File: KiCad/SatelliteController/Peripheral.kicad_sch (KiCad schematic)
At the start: 7 parts, among them J11 RJ45, J15 CONN_AUDIO, J16 CONN_SPEAKER, U2 24LC256, U6 DFPlayer, U7 LTC485CN8#PBF

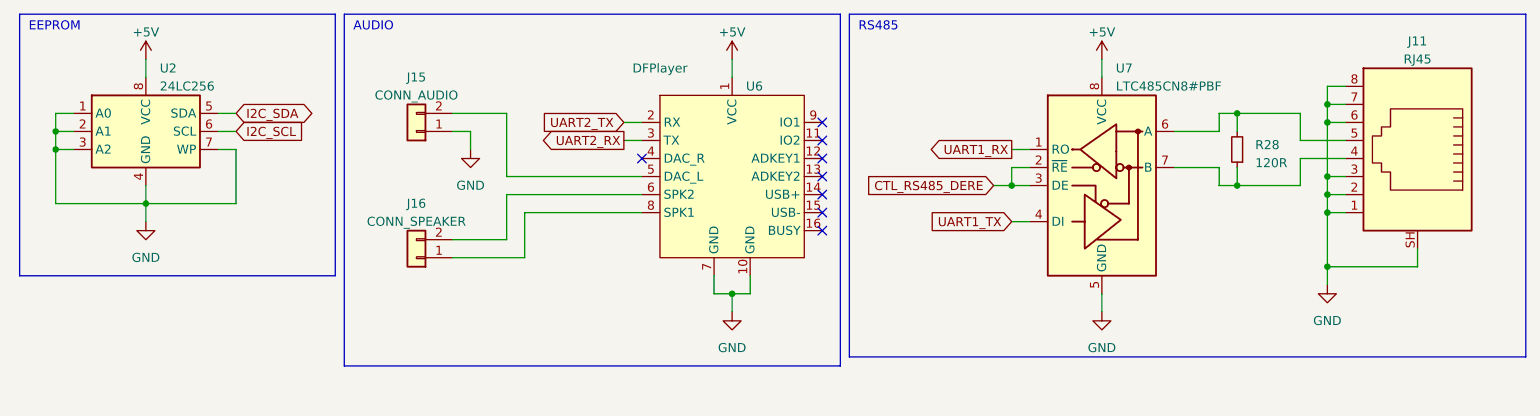
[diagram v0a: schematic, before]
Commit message: 圧力センサとの接続部を追加
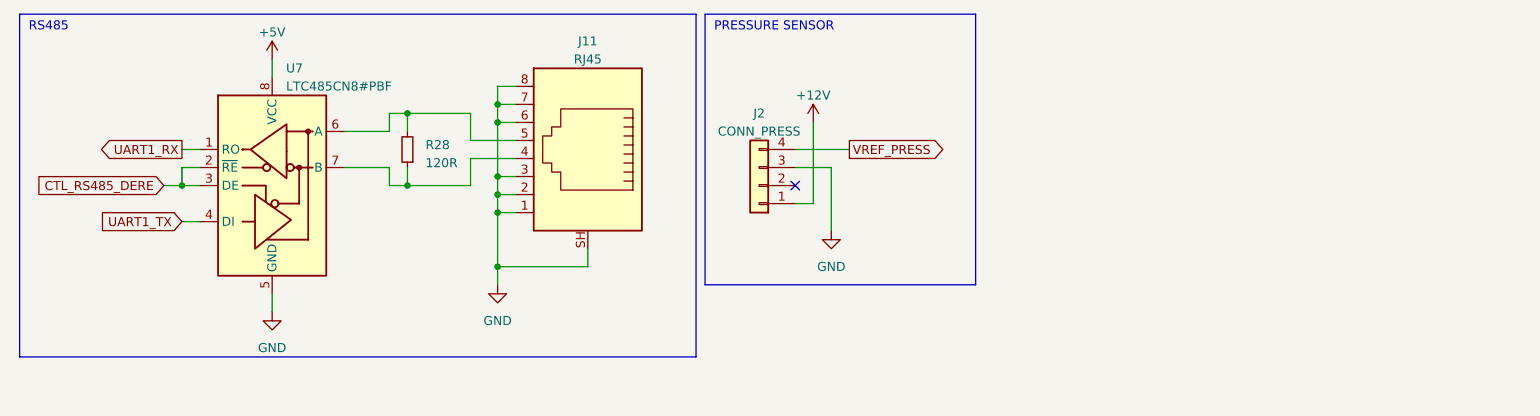
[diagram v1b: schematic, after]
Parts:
- removed J15: CONN_AUDIO, TSRP_TerminalBlock_Alphaplus:TB401-1-2-E, symbol Connector_Generic:Conn_01x02
- removed J16: CONN_SPEAKER, TSRP_TerminalBlock_Alphaplus:TB401-1-2-E, symbol Connector_Generic:Conn_01x02
- removed U2: 24LC256, Package_DIP:DIP-8_W7.62mm, symbol Memory_EEPROM:24LC256
- removed U6: DFPlayer, TSRP_Module:DFPlayer-mini, symbol TSRP_Module:DFPlayer-mini
- added J2: CONN_PRESS, TSRP_TerminalBlock_Alphaplus:TB401-1-4-E, symbol Connector_Generic:Conn_01x04
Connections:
- net GND: now also J2.3 (Pin_3)
- new net +12V: J2.1 (Pin_1)
- new net VREF_PRESS: J2.4 (Pin_4)
- no-connect marks 8 -> 1
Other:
- note added: "PRESSURE SENSOR"
- note removed: "AUDIO"
- note removed: "EEPROM"
- moved on the sheet: J11, R28, U7

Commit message: ランコンのKiCadプロジェクトをコピーしてサテコンを作成
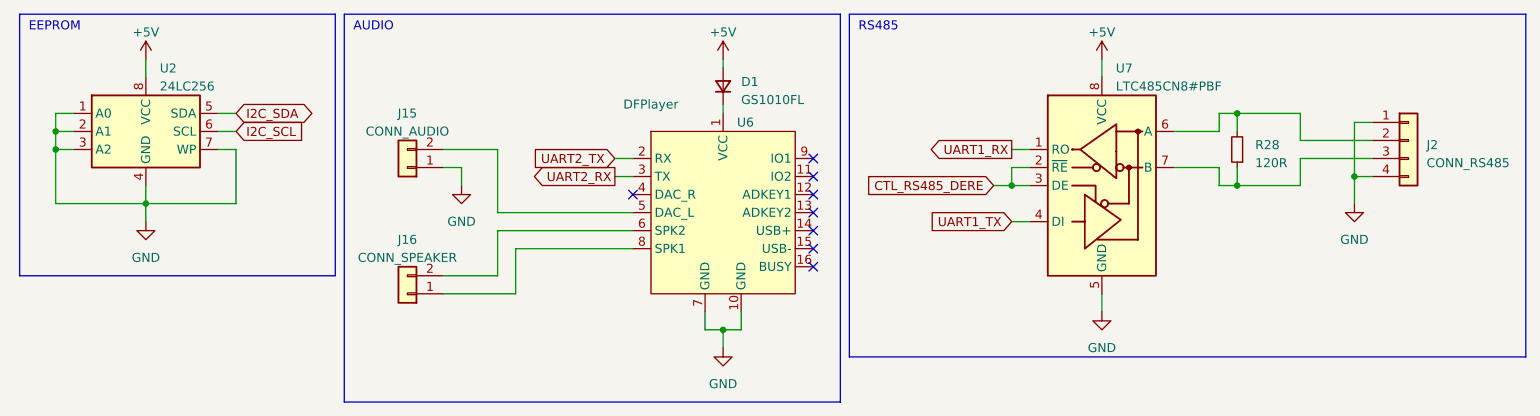
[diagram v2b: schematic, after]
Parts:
- removed J11: RJ45, Connector_RJ:RJ45_Wuerth_7499010001A_Horizontal, symbol Connector:RJ45_Shielded
- added D1: GS1010FL, Diode_SMD:D_SOD-123F, symbol Device:D_Small
- added J15: CONN_AUDIO, TSRP_TerminalBlock_Alphaplus:TB401-1-2-E, symbol Connector_Generic:Conn_01x02
- added J16: CONN_SPEAKER, TSRP_TerminalBlock_Alphaplus:TB401-1-2-E, symbol Connector_Generic:Conn_01x02
- added U2: 24LC256, Package_DIP:DIP-8_W7.62mm, symbol Memory_EEPROM:24LC256
- added U6: DFPlayer, TSRP_Module:DFPlayer-mini, symbol TSRP_Module:DFPlayer-mini
- J2: value CONN_PRESS -> CONN_RS485
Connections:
- net +12V is gone; now on net GND: J2.1 (Pin_1)
- net VREF_PRESS is gone; now on net GND: J2.4 (Pin_4)
- net +5V: now also D1.2 (A), U2.8 (VCC)
- net GND: now also J15.1 (Pin_1), U2.1 (A0), U2.2 (A1), U2.3 (A2), U2.4 (GND), U2.7 (WP), U6.10 (GND), U6.7 (GND); no longer J2.3 (Pin_3)
- net at R28.1, U7.7 (B): now also J2.3 (Pin_3)
- net at R28.2, U7.6 (A): now also J2.2 (Pin_2)
- new net: J16.1 (Pin_1), U6.8 (SPK1)
- new net: J16.2 (Pin_2), U6.6 (SPK2)
- new net: D1.1 (K), U6.1 (VCC)
- new net: J15.2 (Pin_2), U6.5 (DAC_L)
- new net I2C_SCL: U2.6 (SCL)
- new net I2C_SDA: U2.5 (SDA)
- new net UART2_RX: U6.3 (TX)
- new net UART2_TX: U6.2 (RX)
- no-connect marks 1 -> 8
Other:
- note added: "AUDIO"
- note added: "EEPROM"
- note removed: "PRESSURE SENSOR"
- moved on the sheet: R28, U7

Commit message: 音声完成を削除
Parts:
- removed D1: GS1010FL, Diode_SMD:D_SOD-123F, symbol Device:D_Small
- removed J15: CONN_AUDIO, TSRP_TerminalBlock_Alphaplus:TB401-1-2-E, symbol Connector_Generic:Conn_01x02
- removed J16: CONN_SPEAKER, TSRP_TerminalBlock_Alphaplus:TB401-1-2-E, symbol Connector_Generic:Conn_01x02
- removed U6: DFPlayer, TSRP_Module:DFPlayer-mini, symbol TSRP_Module:DFPlayer-mini
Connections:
- no-connect marks 8 -> 0
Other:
- note removed: "AUDIO"

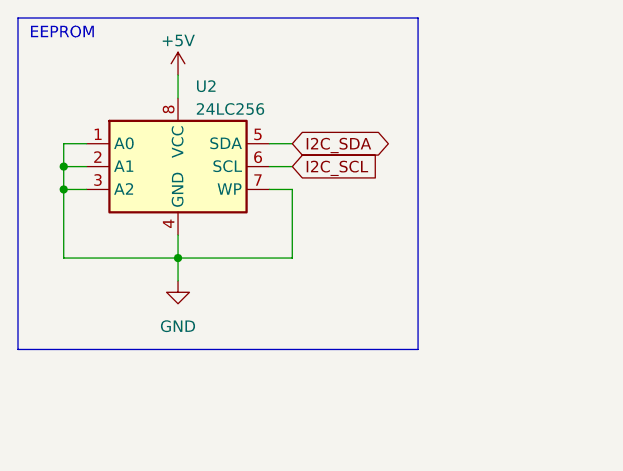
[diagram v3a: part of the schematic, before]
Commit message: 残った手動制御を削除
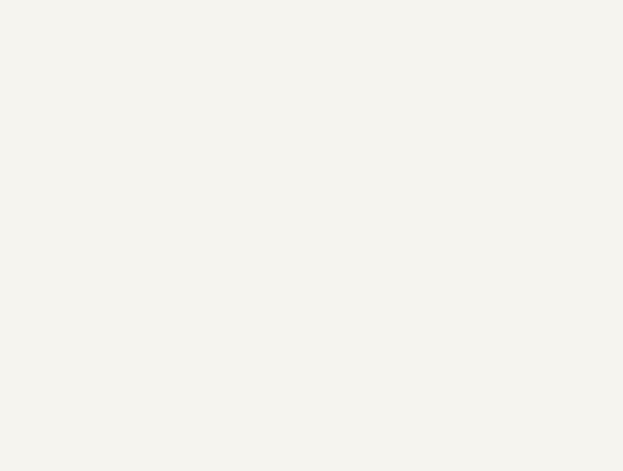
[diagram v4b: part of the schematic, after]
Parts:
- removed U2: 24LC256, Package_DIP:DIP-8_W7.62mm, symbol Memory_EEPROM:24LC256
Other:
- note removed: "EEPROM"
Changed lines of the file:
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@@
 (kicad_sch (version 20230121) (generator eeschema)
   (paper "A4")
-  (junction (at 17.78 29.21) (diameter 0) (color 0 0 0 0)
-  )
   (junction (at 184.15 26.67) (diameter 0) (color 0 0 0 0)
   )
@@
   (junction (at 200.66 35.56) (diameter 0) (color 0 0 0 0)
   )
-  (junction (at 30.48 39.37) (diameter 0) (color 0 0 0 0)
-  )
-  (junction (at 17.78 31.75) (diameter 0) (color 0 0 0 0)
-  )
   (wire (pts (xy 175.26 34.29) (xy 181.61 34.29))
     (stroke (width 0) (type default))
   )
-  (wire (pts (xy 43.18 39.37) (xy 30.48 39.37))
-    (stroke (width 0) (type default))
-  )
   (wire (pts (xy 175.26 29.21) (xy 181.61 29.21))
     (stroke (width 0) (type default))
@@
     (stroke (width 0) (type default))
   )
-  (wire (pts (xy 40.64 26.67) (xy 43.18 26.67))
-    (stroke (width 0) (type default))
-  )
-  (wire (pts (xy 43.18 31.75) (xy 43.18 39.37))
-    (stroke (width 0) (type default))
-  )
   (wire (pts (xy 152.4 36.83) (xy 154.94 36.83))
     (stroke (width 0) (type default))
@@
     (stroke (width 0) (type default))
   )
-  (wire (pts (xy 17.78 39.37) (xy 30.48 39.37))
-    (stroke (width 0) (type default))
-  )
-  (wire (pts (xy 17.78 29.21) (xy 17.78 31.75))
-    (stroke (width 0) (type default))
-  )
   (wire (pts (xy 203.2 27.94) (xy 200.66 27.94))
     (stroke (width 0) (type default))
@@
     (stroke (width 0) (type default))
   )
-  (wire (pts (xy 17.78 26.67) (xy 17.78 29.21))
-    (stroke (width 0) (type default))
-  )
   (wire (pts (xy 181.61 36.83) (xy 184.15 36.83))
     (stroke (width 0) (type default))
   )
-  (wire (pts (xy 40.64 29.21) (xy 43.18 29.21))
-    (stroke (width 0) (type default))
-  )
-  (wire (pts (xy 20.32 29.21) (xy 17.78 29.21))
-    (stroke (width 0) (type default))
-  )
   (wire (pts (xy 200.66 27.94) (xy 200.66 35.56))
     (stroke (width 0) (type default))
@@
     (stroke (width 0) (type default))
   )
-  (wire (pts (xy 30.48 19.05) (xy 30.48 21.59))
-    (stroke (width 0) (type default))
-  )
-  (wire (pts (xy 40.64 31.75) (xy 43.18 31.75))
-    (stroke (width 0) (type default))
-  )
-  (wire (pts (xy 17.78 31.75) (xy 17.78 39.37))
-    (stroke (width 0) (type default))
-  )
   (wire (pts (xy 154.94 34.29) (xy 152.4 34.29))
     (stroke (width 0) (type default))
   )
-  (wire (pts (xy 20.32 31.75) (xy 17.78 31.75))
-    (stroke (width 0) (type default))
-  )
   (wire (pts (xy 181.61 26.67) (xy 184.15 26.67))
     (stroke (width 0) (type default))
@@
     (stroke (width 0) (type default))
   )
-  (wire (pts (xy 20.32 26.67) (xy 17.78 26.67))
-    (stroke (width 0) (type default))
-  )
   (wire (pts (xy 149.86 36.83) (xy 152.4 36.83))
     (stroke (width 0) (type default))
   )
-  (wire (pts (xy 30.48 39.37) (xy 30.48 41.91))
-    (stroke (width 0) (type default))
-  )
-  (wire (pts (xy 30.48 36.83) (xy 30.48 39.37))
-    (stroke (width 0) (type default))
-  )
   (rectangle (start 129.54 12.7) (end 224.79 60.96)
     (stroke (width 0) (type default))
     (fill (type none))
-  )
-  (rectangle (start 12.7 12.7) (end 57.15 49.53)
-    (stroke (width 0) (type default))
-    (fill (type none))
-  )
-  (text "EEPROM" (at 13.97 15.24 0)
-    (effects (font (size 1.27 1.27)) (justify left bottom))
   )
   (text "RS485" (at 130.81 15.24 0)
@@
     )
   )
-  (global_label "I2C_SCL" (shape input) (at 43.18 29.21 0) (fields_autoplaced)
-    (effects (font (size 1.27 1.27)) (justify left))
-    (property "Intersheetrefs" "${INTERSHEET_REFS}" (at 53.6453 29.21 0)
-      (effects (font (size 1.27 1.27)) (justify left) hide)
-    )
-  )
-  (global_label "I2C_SDA" (shape bidirectional) (at 43.18 26.67 0) (fields_autoplaced)
-    (effects (font (size 1.27 1.27)) (justify left))
-    (property "Intersheetrefs" "${INTERSHEET_REFS}" (at 54.8171 26.67 0)
-      (effects (font (size 1.27 1.27)) (justify left) hide)
-    )
-  )
   (global_label "UART1_TX" (shape input) (at 152.4 41.91 180) (fields_autoplaced)
     (effects (font (size 1.27 1.27)) (justify right))
@@
     )
   )
-  (symbol (lib_id "Memory_EEPROM:24LC256") (at 30.48 29.21 0) (unit 1)
-    (in_bom yes) (on_board yes) (dnp no) (fields_autoplaced)
-    (property "Reference" "U2" (at 32.4359 20.32 0)
+  (symbol (lib_id "Connector_Generic:Conn_01x04") (at 208.28 30.48 0) (unit 1)
+    (in_bom yes) (on_board yes) (dnp no) (fields_autoplaced)
+    (property "Reference" "J2" (at 210.82 31.115 0)
       (effects (font (size 1.27 1.27)) (justify left))
     )
-    (property "Value" "24LC256" (at 32.4359 22.86 0)
+    (property "Value" "CONN_RS485" (at 210.82 33.655 0)
       (effects (font (size 1.27 1.27)) (justify left))
     )
-    (property "Footprint" "Package_DIP:DIP-8_W7.62mm" (at 30.48 29.21 0)
-      (effects (font (size 1.27 1.27)) hide)
-    )
-    (property "Datasheet" "https://akizukidenshi.com/catalog/g/gI-00705/" (at 30.48 29.21 0)
-      (effects (font (size 1.27 1.27)) hide)
-    )
-    (property "LCSC" "" (at 30.48 29.21 0)
+    (property "Footprint" "TSRP_TerminalBlock_Alphaplus:TB401-1-4-E" (at 208.28 30.48 0)
+      (effects (font (size 1.27 1.27)) hide)
+    )
+    (property "Datasheet" "https://akizukidenshi.com/catalog/g/gP-07756/" (at 208.28 30.48 0)
+      (effects (font (size 1.27 1.27)) hide)
+    )
+    (property "LCSC" "" (at 208.28 30.48 0)
       (effects (font (size 1.27 1.27)) hide)
     )
@@
     (pin "3")
     (pin "4")
-    (pin "5")
-    (pin "6")
-    (pin "7")
-    (pin "8")
-    (instances
-      (project "SatelliteController"
-        (path "/628d040b-43bf-4733-804f-091644a90124"
-          (reference "U2") (unit 1)
-        )
-        (path "/628d040b-43bf-4733-804f-091644a90124/092bb5f6-479a-4342-8285-14bd550a4a8c"
-          (reference "U7") (unit 1)
-        )
-      )
-    )
-  )
-  (symbol (lib_id "power:+5V") (at 30.48 19.05 0) (unit 1)
-    (in_bom yes) (on_board yes) (dnp no) (fields_autoplaced)
-    (property "Reference" "#PWR014" (at 30.48 22.86 0)
-      (effects (font (size 1.27 1.27)) hide)
-    )
-    (property "Value" "+5V" (at 30.48 15.24 0)
-      (effects (font (size 1.27 1.27)))
-    )
-    (property "Footprint" "" (at 30.48 19.05 0)
-      (effects (font (size 1.27 1.27)) hide)
-    )
-    (property "Datasheet" "" (at 30.48 19.05 0)
-      (effects (font (size 1.27 1.27)) hide)
-    )
-    (pin "1")
-    (instances
-      (project "SatelliteController"
-        (path "/628d040b-43bf-4733-804f-091644a90124"
-          (reference "#PWR014") (unit 1)
-        )
-        (path "/628d040b-43bf-4733-804f-091644a90124/092bb5f6-479a-4342-8285-14bd550a4a8c"
-          (reference "#PWR054") (unit 1)
-        )
-      )
-    )
-  )
-  (symbol (lib_id "Connector_Generic:Conn_01x04") (at 208.28 30.48 0) (unit 1)
-    (in_bom yes) (on_board yes) (dnp no) (fields_autoplaced)
-    (property "Reference" "J2" (at 210.82 31.115 0)
-      (effects (font (size 1.27 1.27)) (justify left))
-    )
-    (property "Value" "CONN_RS485" (at 210.82 33.655 0)
-      (effects (font (size 1.27 1.27)) (justify left))
-    )
-    (property "Footprint" "TSRP_TerminalBlock_Alphaplus:TB401-1-4-E" (at 208.28 30.48 0)
-      (effects (font (size 1.27 1.27)) hide)
-    )
-    (property "Datasheet" "https://akizukidenshi.com/catalog/g/gP-07756/" (at 208.28 30.48 0)
-      (effects (font (size 1.27 1.27)) hide)
-    )
-    (property "LCSC" "" (at 208.28 30.48 0)
-      (effects (font (size 1.27 1.27)) hide)
-    )
-    (pin "1")
-    (pin "2")
-    (pin "3")
-    (pin "4")
     (instances
       (project "SatelliteController"
@@
         )
       )
-    )
-  )
-  (symbol (lib_id "power:GND") (at 30.48 41.91 0) (unit 1)
-    (in_bom yes) (on_board yes) (dnp no) (fields_autoplaced)
-    (property "Reference" "#PWR015" (at 30.48 48.26 0)
-      (effects (font (size 1.27 1.27)) hide)
-    )
-    (property "Value" "GND" (at 30.48 46.99 0)
-      (effects (font (size 1.27 1.27)))
-    )
-    (property "Footprint" "" (at 30.48 41.91 0)
-      (effects (font (size 1.27 1.27)) hide)
-    )
-    (property "Datasheet" "" (at 30.48 41.91 0)
-      (effects (font (size 1.27 1.27)) hide)
-    )
-    (pin "1")
-    (instances
-      (project "SatelliteController"
-        (path "/628d040b-43bf-4733-804f-091644a90124"
-          (reference "#PWR015") (unit 1)
-        )
-        (path "/628d040b-43bf-4733-804f-091644a90124/092bb5f6-479a-4342-8285-14bd550a4a8c"
-          (reference "#PWR058") (unit 1)
-        )
-      )
